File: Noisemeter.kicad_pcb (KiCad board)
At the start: 2 copper layers, 35 x 26 mm, 57 parts, among them IC1 MCP1801, IC2 STM32_48pin, IC3 OPAMP_OS+-D, P1 USB, P2 SWD, P3 MIC2, P4 MOD, X1 32K768 12p5

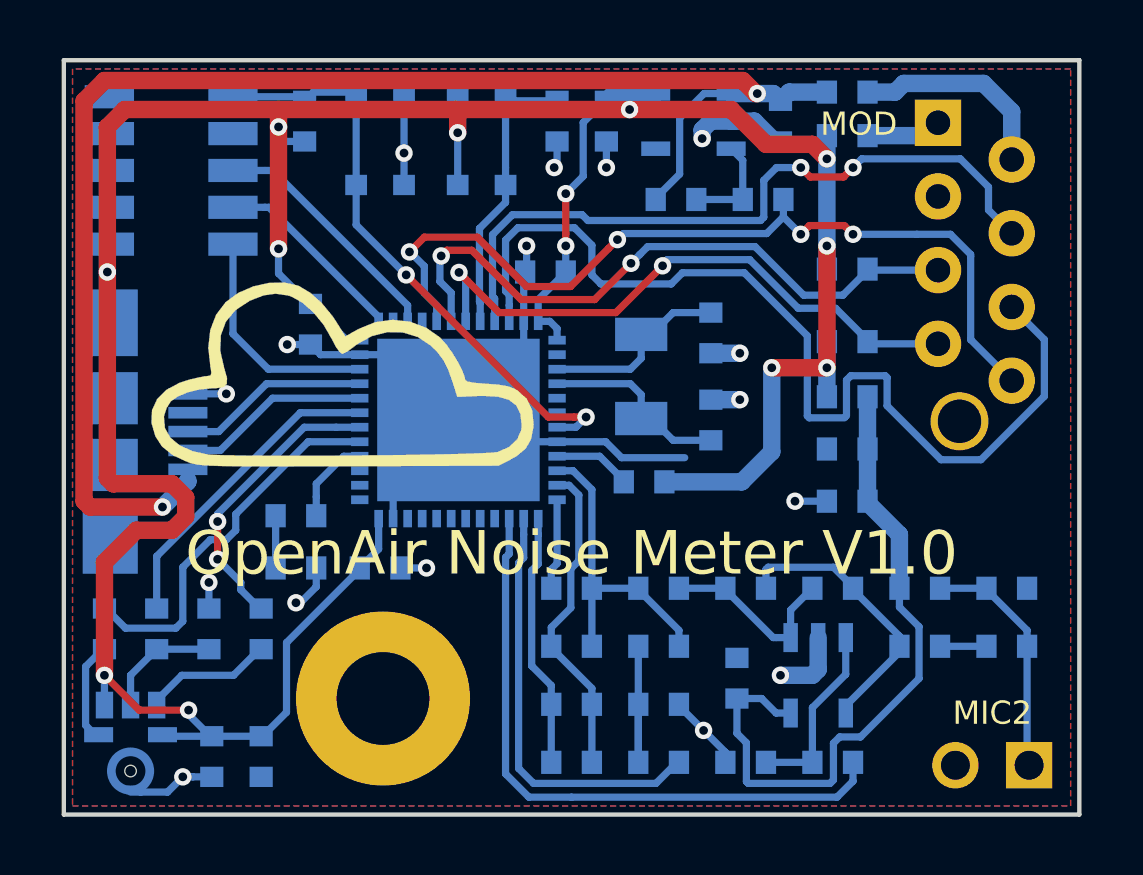
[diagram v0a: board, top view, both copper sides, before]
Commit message: Fixed analog power supply
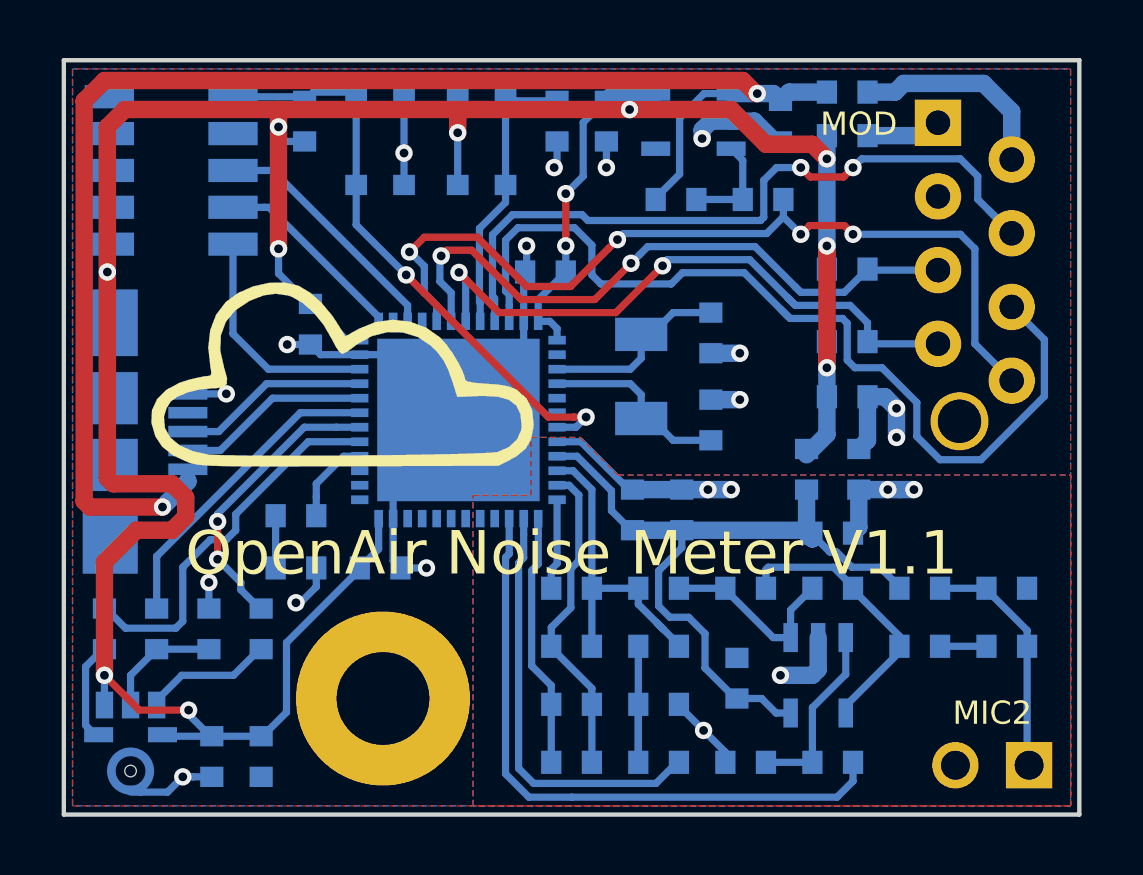
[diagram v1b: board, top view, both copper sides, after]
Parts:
- added C20: 10n, everykey:0603, B.Cu at (74.6, 79.5)
- added C21: 1u, everykey:0603, B.Cu at (76.3, 79.5)
- IC2: value STM32_48pin -> STM32L433Cx
- L1: value FERRITE -> ferrite
- L2: value FERRITE -> 22-47u
- moved L1 7.41 mm to (82.4, 78.1), turned to 270 degrees
- moved C17 3.60 mm to (82.0, 75.6), turned to 0 degrees
- moved C18 2.94 mm to (81.5, 80.3), turned to 0 degrees
- moved L2 2.87 mm to (80.6, 78.1), turned to 270 degrees
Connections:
- C10 pad 2: GND -> AGND
- C13 pad 2: GND -> AGND
- C15 pad 2: GND -> AGND
- C17 pad 1: A3V3 -> 3V3
- C18 pad 2: GND -> AGND
- C19 pad 2: GND -> AGND
- IC2 pad 8: GND -> AGND
- IC2 pad 9: Net-(IC2-Pad9) -> A3V3
- IC3 pad 2: GND -> AGND
- L1 pad 1: Net-(IC2-Pad9) -> GND
- L1 pad 2: 3V3 -> AGND
- P3 pad 2: GND -> AGND
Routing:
- net AGND: track 0.00 -> 15.3 mm, vias 0 -> 6
- net GND: track 51.0 -> 42.4 mm, vias 16 -> 15
- net 3V3: track 114.6 -> 107.9 mm, vias 13 -> 12
- net Net-(IC2-Pad9): track 2.69 -> 0.00 mm
- net ID2: track 34.3 -> 32.1 mm
- net A3V3: track 23.7 -> 25.5 mm
- net SDA: track 20.9 -> 21.5 mm
- added copper zone on B.Cu, net AGND
- added copper zone on F.Cu, net AGND
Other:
- board text added: "OpenAir Noise Meter V1.1"
- board text removed: "OpenAir Noise Meter V1.0"

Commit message: minor changes, BOM rename
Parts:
- moved LOGO1 0.30 mm to (64.6, 74.5)
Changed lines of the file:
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@@
     (links 135)
     (no_connects 0)
-    (area 50.6 63.015 90.461905 91.625)
+    (area 50.6 63.015 90.461905 90.615)
     (thickness 1.6)
     (drawings 5)
@@
     (pad_drill 0.762)
     (pad_to_mask_clearance 0.2)
-    (aux_axis_origin 0 0)
+    (aux_axis_origin 55 64)
     (visible_elements FFFFEF7F)
     (pcbplotparams
-      (layerselection 0x00030_80000001)
+      (layerselection 0x010fc_80000001)
       (usegerberextensions false)
       (excludeedgelayer true)
@@
       (viasonmask false)
       (mode 1)
-      (useauxorigin false)
+      (useauxorigin true)
       (hpglpennumber 1)
       (hpglpenspeed 20)
@@
       (outputformat 1)
       (mirror false)
-      (drillshape 1)
+      (drillshape 0)
       (scaleselection 1)
-      (outputdirectory ""))
+      (outputdirectory Noisemeter_1.1/))
   )
   (net 0 "")
@@
   )
   (module Logo:Logo (layer F.Cu)
-    (at 64.6 74.8)
+    (at 64.6 74.5)
     (fp_text reference LOGO1 (at 0 0) (layer F.SilkS) hide
       (effects (font (thickness 0.3)))
@@
   (module everykey:SPH0645LM4H-B-ext (layer B.Cu)
     (at 57.3 88.5 180)
-    (fp_text reference MIC1 (at 0 -2.05 180) (layer B.SilkS)
-      (effects (font (size 1 1) (thickness 0.15)) (justify mirror))
+    (fp_text reference MIC1 (at 0 1.5 180) (layer F.SilkS)
+      (effects (font (size 0.8 0.8) (thickness 0.15)))
     )
     (fp_text value SPH0645LM4H-B (at 0 3.8 180) (layer B.Fab)
@@
     )
   )
-  (gr_text "OpenAir Noise Meter V1.1\n" (at 72.5 81) (layer F.SilkS)
+  (gr_text "OpenAir Noise Meter V1.1\n" (at 72.5 83.5) (layer F.SilkS)
     (effects (font (size 1.5 1.5) (thickness 0.3)))
   )
